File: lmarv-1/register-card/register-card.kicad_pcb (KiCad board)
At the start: 4 copper layers, 125 x 52.1 mm, 102 parts, among them P1 dual-pcie-cardedge, P2 CONN_01X02, P3 CONN_01X02, U1 74LVTH16374, U2 74LVTH162541, U3 74LVTH162541, U4 74LVTH16374, U5 74LVTH162541, U6 74LVTH162541

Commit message: Updated register card and breakout
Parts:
- added R35: 1k5, Resistors_SMD:R_0603, F.Cu at (146.9, 138.8)
- C1, C10, C11, C12, C13, C14, C15, C16, C17, C18, C19, C2, C20, C21, C22, C23, C24, C3, C4, C5, C6, C7, C8, C9: moved to F.Cu
- P2, P3: footprint Pin_Headers:Pin_Header_Straight_1x02_Pitch2.54mm -> Pin_Headers:Pin_Header_Straight_1x02_Pitch1.27mm
- REF***: moved to B.Cu
- U1, U4: value 74LVTH16374 -> 74LVT16374
- U2, U3, U5, U6: value 74LVTH162541 -> 74LVT16374
- moved C17 85.9 mm to (161.8, 139.6), turned to 0 degrees
- moved C19 78.2 mm to (155.0, 139.6), turned to 0 degrees
- moved U1 77.5 mm to (134.2, 146.4)
- moved U4 76.1 mm to (157.6, 146.4)
- moved C18 74.8 mm to (161.1, 153.9), turned to 270 degrees
- moved C20 67.3 mm to (154.1, 153.9)
- moved C13 46.7 mm to (138.6, 139.4), turned to 0 degrees
- moved C15 39.1 mm to (131.5, 139.4), turned to 0 degrees
- moved C14 38.4 mm to (137.7, 153.9), turned to 270 degrees
- moved C16 32.4 mm to (130.7, 153.8)
- moved C1 27.8 mm to (53.4, 139.6), turned to 0 degrees
- moved C5 26.9 mm to (80.4, 139.5), turned to 0 degrees
- moved C3 24.7 mm to (46.2, 139.6), turned to 0 degrees
- moved C6 23.6 mm to (79.0, 153.0), turned to 180 degrees
- moved C9 23.2 mm to (97.0, 138.9), turned to 90 degrees
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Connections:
- D1 pad 1: Net-(D1-Pad1) -> GNDREF
- D10 pad 1: Net-(D1-Pad1) -> GNDREF
- D11 pad 1: Net-(D1-Pad1) -> GNDREF
- D12 pad 1: Net-(D1-Pad1) -> GNDREF
- D13 pad 1: Net-(D1-Pad1) -> GNDREF
- D14 pad 1: Net-(D1-Pad1) -> GNDREF
- D15 pad 1: Net-(D1-Pad1) -> GNDREF
- D16 pad 1: Net-(D1-Pad1) -> GNDREF
- D17 pad 1: Net-(D1-Pad1) -> GNDREF
- D18 pad 1: Net-(D1-Pad1) -> GNDREF
- D19 pad 1: Net-(D1-Pad1) -> GNDREF
- D2 pad 1: Net-(D1-Pad1) -> GNDREF
- D20 pad 1: Net-(D1-Pad1) -> GNDREF
- D21 pad 1: Net-(D1-Pad1) -> GNDREF
- D22 pad 1: Net-(D1-Pad1) -> GNDREF
- D23 pad 1: Net-(D1-Pad1) -> GNDREF
- D24 pad 1: Net-(D1-Pad1) -> GNDREF
- D25 pad 1: Net-(D1-Pad1) -> GNDREF
- D26 pad 1: Net-(D1-Pad1) -> GNDREF
- D27 pad 1: Net-(D1-Pad1) -> GNDREF
- D28 pad 1: Net-(D1-Pad1) -> GNDREF
- D29 pad 1: Net-(D1-Pad1) -> GNDREF
- D3 pad 1: Net-(D1-Pad1) -> GNDREF
- D30 pad 1: Net-(D1-Pad1) -> GNDREF
- D31 pad 1: Net-(D1-Pad1) -> GNDREF
- D32 pad 1: Net-(D1-Pad1) -> GNDREF
- D4 pad 1: Net-(D1-Pad1) -> GNDREF
- D5 pad 1: Net-(D1-Pad1) -> GNDREF
- D6 pad 1: Net-(D1-Pad1) -> GNDREF
- D7 pad 1: Net-(D1-Pad1) -> GNDREF
- D8 pad 1: Net-(D1-Pad1) -> GNDREF
- D9 pad 1: Net-(D1-Pad1) -> GNDREF
- P2 pad 2: Net-(D1-Pad1) -> Net-(P2-Pad2)
- U1 pad 1: GNDREF -> /~rs1oe
- U1 pad 11: /rdq[22] -> /rs1[22]
- U1 pad 12: /rdq[23] -> /rs1[23]
- U1 pad 13: /rdq[24] -> /rs1[24]
- U1 pad 14: /rdq[25] -> /rs1[25]
- U1 pad 16: /rdq[26] -> /rs1[26]
- U1 pad 17: /rdq[27] -> /rs1[27]
- U1 pad 19: /rdq[28] -> /rs1[28]
- U1 pad 2: /rdq[16] -> /rs1[16]
- U1 pad 20: /rdq[29] -> /rs1[29]
- U1 pad 22: /rdq[30] -> /rs1[30]
- U1 pad 23: /rdq[31] -> /rs1[31]
- U1 pad 24: GNDREF -> /~rs1oe
- U1 pad 3: /rdq[17] -> /rs1[17]
- U1 pad 5: /rdq[18] -> /rs1[18]
- U1 pad 6: /rdq[19] -> /rs1[19]
- U1 pad 8: /rdq[20] -> /rs1[20]
- U1 pad 9: /rdq[21] -> /rs1[21]
- U2 pad 25: /~rs2oe -> /rdclk
- U2 pad 26: /rdq[31] -> /rd[31]
- U2 pad 27: /rdq[30] -> /rd[30]
- U2 pad 29: /rdq[29] -> /rd[29]
- U2 pad 30: /rdq[28] -> /rd[28]
- U2 pad 32: /rdq[27] -> /rd[27]
- U2 pad 33: /rdq[26] -> /rd[26]
- U2 pad 35: /rdq[25] -> /rd[25]
- U2 pad 36: /rdq[24] -> /rd[24]
- U2 pad 37: /rdq[23] -> /rd[23]
- U2 pad 38: /rdq[22] -> /rd[22]
- U2 pad 40: /rdq[21] -> /rd[21]
- U2 pad 41: /rdq[20] -> /rd[20]
- U2 pad 43: /rdq[19] -> /rd[19]
- U2 pad 44: /rdq[18] -> /rd[18]
- U2 pad 46: /rdq[17] -> /rd[17]
- U2 pad 47: /rdq[16] -> /rd[16]
- U2 pad 48: /~rs2oe -> /rdclk
- U3 pad 1: /~rs2oe -> Net-(P2-Pad2)
- U3 pad 11: /rs2[6] -> /rdq[22]
- U3 pad 12: /rs2[7] -> /rdq[23]
- U3 pad 13: /rs2[8] -> /rdq[24]
- U3 pad 14: /rs2[9] -> /rdq[25]
- U3 pad 16: /rs2[10] -> /rdq[26]
- U3 pad 17: /rs2[11] -> /rdq[27]
- U3 pad 19: /rs2[12] -> /rdq[28]
- U3 pad 2: /rs2[0] -> /rdq[16]
- U3 pad 20: /rs2[13] -> /rdq[29]
- U3 pad 22: /rs2[14] -> /rdq[30]
- U3 pad 23: /rs2[15] -> /rdq[31]
- U3 pad 24: /~rs2oe -> Net-(P2-Pad2)
- U3 pad 25: /~rs2oe -> /rdclk
- U3 pad 26: /rdq[15] -> /rd[31]
- U3 pad 27: /rdq[14] -> /rd[30]
- U3 pad 29: /rdq[13] -> /rd[29]
- U3 pad 3: /rs2[1] -> /rdq[17]
- U3 pad 30: /rdq[12] -> /rd[28]
- U3 pad 32: /rdq[11] -> /rd[27]
- U3 pad 33: /rdq[10] -> /rd[26]
- U3 pad 35: /rdq[9] -> /rd[25]
- U3 pad 36: /rdq[8] -> /rd[24]
- U3 pad 37: /rdq[7] -> /rd[23]
- U3 pad 38: /rdq[6] -> /rd[22]
- U3 pad 40: /rdq[5] -> /rd[21]
- U3 pad 41: /rdq[4] -> /rd[20]
- U3 pad 43: /rdq[3] -> /rd[19]
- U3 pad 44: /rdq[2] -> /rd[18]
- U3 pad 46: /rdq[1] -> /rd[17]
- U3 pad 47: /rdq[0] -> /rd[16]
- U3 pad 48: /~rs2oe -> /rdclk
- U3 pad 5: /rs2[2] -> /rdq[18]
- U3 pad 6: /rs2[3] -> /rdq[19]
- U3 pad 8: /rs2[4] -> /rdq[20]
- U3 pad 9: /rs2[5] -> /rdq[21]
- U4 pad 1: GNDREF -> /~rs1oe
- U4 pad 11: /rdq[6] -> /rs1[6]
- U4 pad 12: /rdq[7] -> /rs1[7]
- U4 pad 13: /rdq[8] -> /rs1[8]
- U4 pad 14: /rdq[9] -> /rs1[9]
- U4 pad 16: /rdq[10] -> /rs1[10]
- U4 pad 17: /rdq[11] -> /rs1[11]
- U4 pad 19: /rdq[12] -> /rs1[12]
- U4 pad 2: /rdq[0] -> /rs1[0]
- U4 pad 20: /rdq[13] -> /rs1[13]
- U4 pad 22: /rdq[14] -> /rs1[14]
- U4 pad 23: /rdq[15] -> /rs1[15]
- U4 pad 24: GNDREF -> /~rs1oe
- U4 pad 3: /rdq[1] -> /rs1[1]
- U4 pad 5: /rdq[2] -> /rs1[2]
- U4 pad 6: /rdq[3] -> /rs1[3]
- U4 pad 8: /rdq[4] -> /rs1[4]
- U4 pad 9: /rdq[5] -> /rs1[5]
- U5 pad 1: /~rs1oe -> /~rs2oe
- U5 pad 11: /rs1[22] -> /rs2[6]
- U5 pad 12: /rs1[23] -> /rs2[7]
- U5 pad 13: /rs1[24] -> /rs2[8]
- U5 pad 14: /rs1[25] -> /rs2[9]
- U5 pad 16: /rs1[26] -> /rs2[10]
- U5 pad 17: /rs1[27] -> /rs2[11]
- U5 pad 19: /rs1[28] -> /rs2[12]
- U5 pad 2: /rs1[16] -> /rs2[0]
- U5 pad 20: /rs1[29] -> /rs2[13]
- U5 pad 22: /rs1[30] -> /rs2[14]
- U5 pad 23: /rs1[31] -> /rs2[15]
- U5 pad 24: /~rs1oe -> /~rs2oe
- U5 pad 25: /~rs1oe -> /rdclk
- U5 pad 26: /rdq[31] -> /rd[15]
- U5 pad 27: /rdq[30] -> /rd[14]
- U5 pad 29: /rdq[29] -> /rd[13]
- U5 pad 3: /rs1[17] -> /rs2[1]
- U5 pad 30: /rdq[28] -> /rd[12]
- U5 pad 32: /rdq[27] -> /rd[11]
- U5 pad 33: /rdq[26] -> /rd[10]
- U5 pad 35: /rdq[25] -> /rd[9]
- U5 pad 36: /rdq[24] -> /rd[8]
- U5 pad 37: /rdq[23] -> /rd[7]
- U5 pad 38: /rdq[22] -> /rd[6]
- U5 pad 40: /rdq[21] -> /rd[5]
- U5 pad 41: /rdq[20] -> /rd[4]
- U5 pad 43: /rdq[19] -> /rd[3]
- U5 pad 44: /rdq[18] -> /rd[2]
- U5 pad 46: /rdq[17] -> /rd[1]
- U5 pad 47: /rdq[16] -> /rd[0]
- U5 pad 48: /~rs1oe -> /rdclk
- U5 pad 5: /rs1[18] -> /rs2[2]
- U5 pad 6: /rs1[19] -> /rs2[3]
- U5 pad 8: /rs1[20] -> /rs2[4]
- U5 pad 9: /rs1[21] -> /rs2[5]
- U6 pad 1: /~rs1oe -> Net-(P2-Pad2)
- U6 pad 11: /rs1[6] -> /rdq[6]
- U6 pad 12: /rs1[7] -> /rdq[7]
- U6 pad 13: /rs1[8] -> /rdq[8]
- U6 pad 14: /rs1[9] -> /rdq[9]
- U6 pad 16: /rs1[10] -> /rdq[10]
- U6 pad 17: /rs1[11] -> /rdq[11]
- U6 pad 19: /rs1[12] -> /rdq[12]
- U6 pad 2: /rs1[0] -> /rdq[0]
- U6 pad 20: /rs1[13] -> /rdq[13]
- U6 pad 22: /rs1[14] -> /rdq[14]
- U6 pad 23: /rs1[15] -> /rdq[15]
- U6 pad 24: /~rs1oe -> Net-(P2-Pad2)
- U6 pad 25: /~rs1oe -> /rdclk
- U6 pad 26: /rdq[15] -> /rd[15]
- U6 pad 27: /rdq[14] -> /rd[14]
- U6 pad 29: /rdq[13] -> /rd[13]
- U6 pad 3: /rs1[1] -> /rdq[1]
- U6 pad 30: /rdq[12] -> /rd[12]
- U6 pad 32: /rdq[11] -> /rd[11]
- U6 pad 33: /rdq[10] -> /rd[10]
- U6 pad 35: /rdq[9] -> /rd[9]
- U6 pad 36: /rdq[8] -> /rd[8]
- U6 pad 37: /rdq[7] -> /rd[7]
- U6 pad 38: /rdq[6] -> /rd[6]
- U6 pad 40: /rdq[5] -> /rd[5]
- U6 pad 41: /rdq[4] -> /rd[4]
- U6 pad 43: /rdq[3] -> /rd[3]
- U6 pad 44: /rdq[2] -> /rd[2]
- U6 pad 46: /rdq[1] -> /rd[1]
- U6 pad 47: /rdq[0] -> /rd[0]
- U6 pad 48: /~rs1oe -> /rdclk
- U6 pad 5: /rs1[2] -> /rdq[2]
- U6 pad 6: /rs1[3] -> /rdq[3]
- U6 pad 8: /rs1[4] -> /rdq[4]
- U6 pad 9: /rs1[5] -> /rdq[5]
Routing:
- net /rdclk: track 55.2 -> 256.7 mm, vias 0 -> 10
- net /rd[31]: track 11.5 -> 162.8 mm, vias 0 -> 3
- net /rd[29]: track 11.1 -> 160.0 mm, vias 0 -> 3
- net /rd[30]: track 11.4 -> 159.8 mm, vias 0 -> 3
- net /rd[28]: track 10.9 -> 158.8 mm, vias 0 -> 3
- net /rd[23]: track 10.3 -> 157.8 mm, vias 0 -> 3
- net /rd[27]: track 10.6 -> 157.5 mm, vias 0 -> 3
- net /rd[24]: track 10.0 -> 156.2 mm, vias 0 -> 3
- net /rd[22]: track 10.4 -> 155.9 mm, vias 0 -> 3
- net /rd[25]: track 10.2 -> 155.5 mm, vias 0 -> 3
- net /rd[20]: track 10.9 -> 155.9 mm, vias 0 -> 3
- net /rd[26]: track 10.5 -> 155.5 mm, vias 0 -> 3
- net /rd[21]: track 10.7 -> 155.2 mm, vias 0 -> 3
- net /rd[19]: track 11.3 -> 155.6 mm, vias 0 -> 3
- net /rd[18]: track 11.4 -> 155.5 mm, vias 0 -> 3
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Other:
- board size 125 x 52.1 mm -> 126.5 x 57.1 mm
- board text added: "ANODES (+)"
- board text added: "CATHODES (-)"
- board text added: "DISPLAY STORAGE"
- board text added: "RS1OE"
- board text added: "RS2OE"
- board text added: "SOURCE 1 STORAGE"
- board text added: "SOURCE 2 STORAGE"
- board text added: "https://github.com/RobertBaruch/lmarv REV B 2018 JAN 23 LMARV-1 32-BIT REGISTER"
- board text removed: "ANODES"
- board text removed: "CATHODES"
- board text removed: "LMARV 1 32-BIT REGISTER"
- board text removed: "REV B 2018 JAN 20"
- board text removed: "RS1~OE"
- board text removed: "RS2~OE"

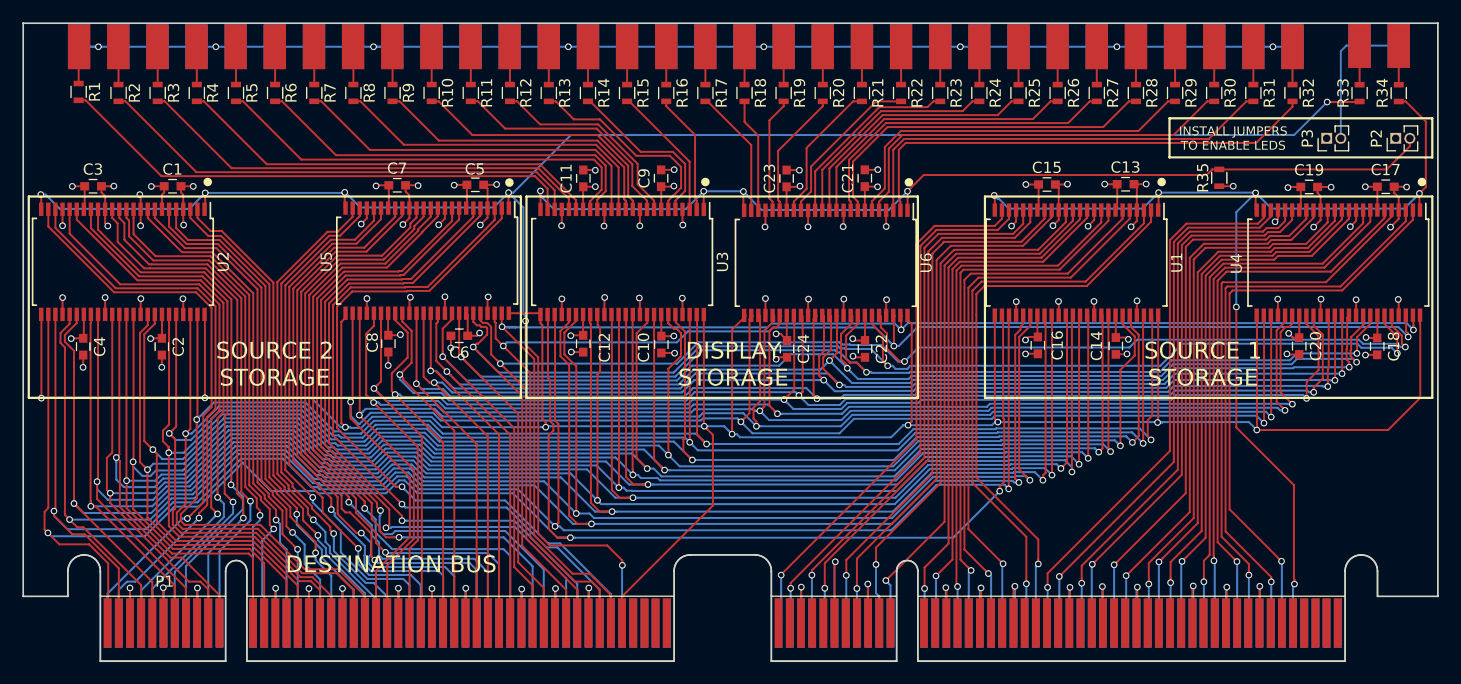
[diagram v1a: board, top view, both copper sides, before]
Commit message: Adds RAM-based register card
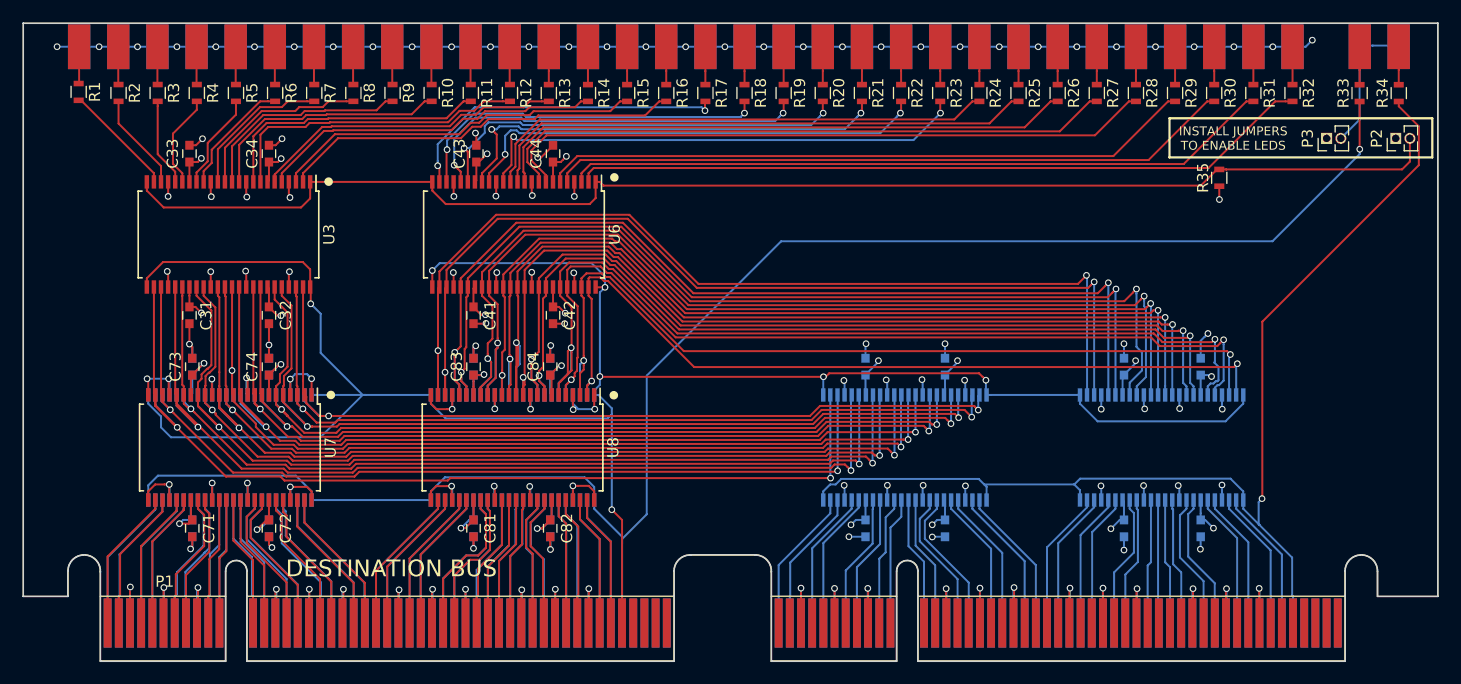
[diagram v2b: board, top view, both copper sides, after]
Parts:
- removed C1, C10, C15, C16, C17, C18, C19, C2, C20, C3, C4, C5, C6, C7, C8, C9: 100n, Capacitors_SMD:C_0603
- added C31: 100n, Capacitors_SMD:C_0603, F.Cu at (54.9, 151.1)
- added C32: 100n, Capacitors_SMD:C_0603, F.Cu at (62.0, 151.1)
- added C33: 100n, Capacitors_SMD:C_0603, F.Cu at (54.9, 136.7)
- added C34: 100n, Capacitors_SMD:C_0603, F.Cu at (62.0, 136.7)
- added C41: 100n, Capacitors_SMD:C_0603, F.Cu at (80.3, 151.1)
- added C42: 100n, Capacitors_SMD:C_0603, F.Cu at (87.4, 151.1)
- added C43: 100n, Capacitors_SMD:C_0603, F.Cu at (80.5, 136.7)
- added C44: 100n, Capacitors_SMD:C_0603, F.Cu at (87.4, 136.7)
- added C51: 100n, Capacitors_SMD:C_0603, B.Cu at (80.3, 170.2)
- added C52: 100n, Capacitors_SMD:C_0603, B.Cu at (87.1, 170.2)
- added C53: 100n, Capacitors_SMD:C_0603, B.Cu at (80.3, 155.7)
- added C54: 100n, Capacitors_SMD:C_0603, B.Cu at (87.1, 155.7)
- added C61: 100n, Capacitors_SMD:C_0603, B.Cu at (138.4, 170.2)
- added C62: 100n, Capacitors_SMD:C_0603, B.Cu at (145.3, 170.2)
- added C63: 100n, Capacitors_SMD:C_0603, B.Cu at (138.4, 155.7)
- added C64: 100n, Capacitors_SMD:C_0603, B.Cu at (145.3, 155.7)
- added C71: 100n, Capacitors_SMD:C_0603, F.Cu at (55.1, 170.2)
- added C72: 100n, Capacitors_SMD:C_0603, F.Cu at (62.0, 170.2)
- added C73: 100n, Capacitors_SMD:C_0603, F.Cu at (55.1, 155.7)
- added C74: 100n, Capacitors_SMD:C_0603, F.Cu at (62.0, 155.7)
- added C81: 100n, Capacitors_SMD:C_0603, F.Cu at (80.3, 170.2)
- added C82: 100n, Capacitors_SMD:C_0603, F.Cu at (87.1, 170.2)
- added C83: 100n, Capacitors_SMD:C_0603, F.Cu at (80.3, 155.7)
- added C84: 100n, Capacitors_SMD:C_0603, F.Cu at (87.1, 155.7)
- added U7: 74LVT162244, Housings_SSOP:SSOP-48_7.5x15.9mm_Pitch0.635mm, F.Cu at (58.5, 162.9)
- added U8: 74LVT162244, Housings_SSOP:SSOP-48_7.5x15.9mm_Pitch0.635mm, F.Cu at (83.8, 162.9)
- C11, C12, C13, C14, C21, C22, C23, C24, U1, U2, U4, U5: moved to B.Cu
- moved C21 67.8 mm to (55.1, 170.2), turned to 270 degrees
- moved C23 55.7 mm to (55.1, 155.7)
- moved C22 55.7 mm to (62.0, 170.2)
- moved C24 46.4 mm to (62.0, 155.7), turned to 90 degrees
- moved C11 40.2 mm to (115.3, 170.2), turned to 270 degrees
- moved C12 36.3 mm to (122.4, 170.2)
- moved U3 35.3 mm to (58.4, 143.9)
- moved C13 28.4 mm to (115.3, 155.7), turned to 90 degrees
- moved U6 28.0 mm to (83.9, 143.9)
- moved U4 22.9 mm to (141.8, 162.9), turned to 90 degrees
- moved U1 22.6 mm to (118.8, 162.9), turned to 90 degrees
- moved U2 19.2 mm to (58.5, 162.9), turned to 90 degrees
- moved U5 18.4 mm to (83.8, 162.9), turned to 90 degrees
- moved C14 15.4 mm to (122.4, 155.7), turned to 90 degrees
- moved REF*** 12.2 mm to (156.7, 156.9)
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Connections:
- net Net-(P2-Pad2) renamed //LEDOE
- U1 pad 26: /rd[31] -> /dd[31]
- U1 pad 27: /rd[30] -> /dd[30]
- U1 pad 29: /rd[29] -> /dd[29]
- U1 pad 30: /rd[28] -> /dd[28]
- U1 pad 32: /rd[27] -> /dd[27]
- U1 pad 33: /rd[26] -> /dd[26]
- U1 pad 35: /rd[25] -> /dd[25]
- U1 pad 36: /rd[24] -> /dd[24]
- U1 pad 37: /rd[23] -> /dd[23]
- U1 pad 38: /rd[22] -> /dd[22]
- U1 pad 40: /rd[21] -> /dd[21]
- U1 pad 41: /rd[20] -> /dd[20]
- U1 pad 43: /rd[19] -> /dd[19]
- U1 pad 44: /rd[18] -> /dd[18]
- U1 pad 46: /rd[17] -> /dd[17]
- U1 pad 47: /rd[16] -> /dd[16]
- U2 pad 26: /rd[31] -> /dd[31]
- U2 pad 27: /rd[30] -> /dd[30]
- U2 pad 29: /rd[29] -> /dd[29]
- U2 pad 30: /rd[28] -> /dd[28]
- U2 pad 32: /rd[27] -> /dd[27]
- U2 pad 33: /rd[26] -> /dd[26]
- U2 pad 35: /rd[25] -> /dd[25]
- U2 pad 36: /rd[24] -> /dd[24]
- U2 pad 37: /rd[23] -> /dd[23]
- U2 pad 38: /rd[22] -> /dd[22]
- U2 pad 40: /rd[21] -> /dd[21]
- U2 pad 41: /rd[20] -> /dd[20]
- U2 pad 43: /rd[19] -> /dd[19]
- U2 pad 44: /rd[18] -> /dd[18]
- U2 pad 46: /rd[17] -> /dd[17]
- U2 pad 47: /rd[16] -> /dd[16]
- U3 pad 26: /rd[31] -> /dd[31]
- U3 pad 27: /rd[30] -> /dd[30]
- U3 pad 29: /rd[29] -> /dd[29]
- U3 pad 30: /rd[28] -> /dd[28]
- U3 pad 32: /rd[27] -> /dd[27]
- U3 pad 33: /rd[26] -> /dd[26]
- U3 pad 35: /rd[25] -> /dd[25]
- U3 pad 36: /rd[24] -> /dd[24]
- U3 pad 37: /rd[23] -> /dd[23]
- U3 pad 38: /rd[22] -> /dd[22]
- U3 pad 40: /rd[21] -> /dd[21]
- U3 pad 41: /rd[20] -> /dd[20]
- U3 pad 43: /rd[19] -> /dd[19]
- U3 pad 44: /rd[18] -> /dd[18]
- U3 pad 46: /rd[17] -> /dd[17]
- U3 pad 47: /rd[16] -> /dd[16]
- U4 pad 26: /rd[15] -> /dd[15]
- U4 pad 27: /rd[14] -> /dd[14]
- U4 pad 29: /rd[13] -> /dd[13]
- U4 pad 30: /rd[12] -> /dd[12]
- U4 pad 32: /rd[11] -> /dd[11]
- U4 pad 33: /rd[10] -> /dd[10]
- U4 pad 35: /rd[9] -> /dd[9]
- U4 pad 36: /rd[8] -> /dd[8]
- U4 pad 37: /rd[7] -> /dd[7]
- U4 pad 38: /rd[6] -> /dd[6]
- U4 pad 40: /rd[5] -> /dd[5]
- U4 pad 41: /rd[4] -> /dd[4]
- U4 pad 43: /rd[3] -> /dd[3]
- U4 pad 44: /rd[2] -> /dd[2]
- U4 pad 46: /rd[1] -> /dd[1]
- U4 pad 47: /rd[0] -> /dd[0]
- U5 pad 26: /rd[15] -> /dd[15]
- U5 pad 27: /rd[14] -> /dd[14]
- U5 pad 29: /rd[13] -> /dd[13]
- U5 pad 30: /rd[12] -> /dd[12]
- U5 pad 32: /rd[11] -> /dd[11]
- U5 pad 33: /rd[10] -> /dd[10]
- U5 pad 35: /rd[9] -> /dd[9]
- U5 pad 36: /rd[8] -> /dd[8]
- U5 pad 37: /rd[7] -> /dd[7]
- U5 pad 38: /rd[6] -> /dd[6]
- U5 pad 40: /rd[5] -> /dd[5]
- U5 pad 41: /rd[4] -> /dd[4]
- U5 pad 43: /rd[3] -> /dd[3]
- U5 pad 44: /rd[2] -> /dd[2]
- U5 pad 46: /rd[1] -> /dd[1]
- U5 pad 47: /rd[0] -> /dd[0]
- U6 pad 26: /rd[15] -> /dd[15]
- U6 pad 27: /rd[14] -> /dd[14]
- U6 pad 29: /rd[13] -> /dd[13]
- U6 pad 30: /rd[12] -> /dd[12]
- U6 pad 32: /rd[11] -> /dd[11]
- U6 pad 33: /rd[10] -> /dd[10]
- U6 pad 35: /rd[9] -> /dd[9]
- U6 pad 36: /rd[8] -> /dd[8]
- U6 pad 37: /rd[7] -> /dd[7]
- U6 pad 38: /rd[6] -> /dd[6]
- U6 pad 40: /rd[5] -> /dd[5]
- U6 pad 41: /rd[4] -> /dd[4]
- U6 pad 43: /rd[3] -> /dd[3]
- U6 pad 44: /rd[2] -> /dd[2]
- U6 pad 46: /rd[1] -> /dd[1]
- U6 pad 47: /rd[0] -> /dd[0]
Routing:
- net /rd[31]: track 162.8 -> 12.8 mm, vias 3 -> 0
- net /rd[29]: track 160.0 -> 12.3 mm, vias 3 -> 0
- net /rd[30]: track 159.8 -> 12.6 mm, vias 3 -> 0
- net /rd[28]: track 158.8 -> 12.2 mm, vias 3 -> 0
- net /rd[23]: track 157.8 -> 11.7 mm, vias 3 -> 0
- net /rd[27]: track 157.5 -> 12.3 mm, vias 3 -> 0
- net /rd[24]: track 156.2 -> 11.3 mm, vias 3 -> 0
- net /rd[25]: track 155.5 -> 11.4 mm, vias 3 -> 0
- net /rd[22]: track 155.9 -> 11.9 mm, vias 3 -> 0
- net /rd[26]: track 155.5 -> 12.0 mm, vias 3 -> 0
- net /rd[19]: track 155.6 -> 12.6 mm, vias 3 -> 0
- net /rd[18]: track 155.5 -> 12.8 mm, vias 3 -> 0
- net /rd[20]: track 155.9 -> 13.2 mm, vias 3 -> 0
- net /rd[21]: track 155.2 -> 12.8 mm, vias 3 -> 0
- net /rd[17]: track 153.6 -> 13.1 mm, vias 3 -> 0
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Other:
- board text added: "https://github.com/RobertBaruch/lmarv REV C 2018 MAY 17 LMARV-1 32-BIT REGISTER"
- board text removed: "DISPLAY STORAGE"
- board text removed: "SOURCE 1 STORAGE"
- board text removed: "SOURCE 2 STORAGE"
- board text removed: "https://github.com/RobertBaruch/lmarv REV B 2018 JAN 23 LMARV-1 32-BIT REGISTER"
